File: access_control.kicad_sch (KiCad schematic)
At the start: 72 parts, among them J1 Conn_01x04_Pin, J10 Screw_Terminal_01x02, J2 Screw_Terminal_01x04, J3 Screw_Terminal_01x04, J4 Screw_Terminal_01x02, J5 Screw_Terminal_01x04, J6 Screw_Terminal_01x04, J7 Screw_Terminal_01x02, J8 Screw_Terminal_01x02, J9 Screw_Terminal_01x02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

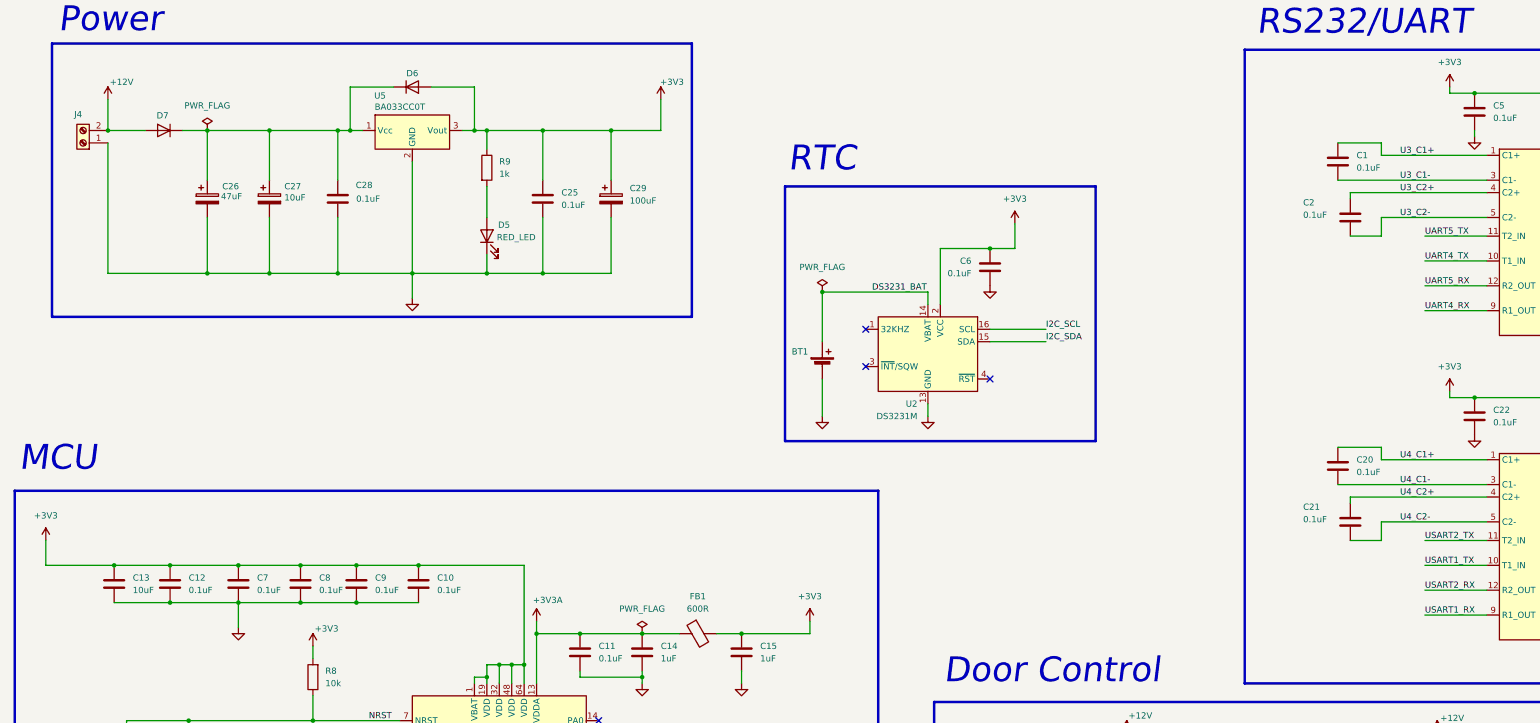
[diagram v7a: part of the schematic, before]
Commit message: Finished the PCB routing and placement of the components.
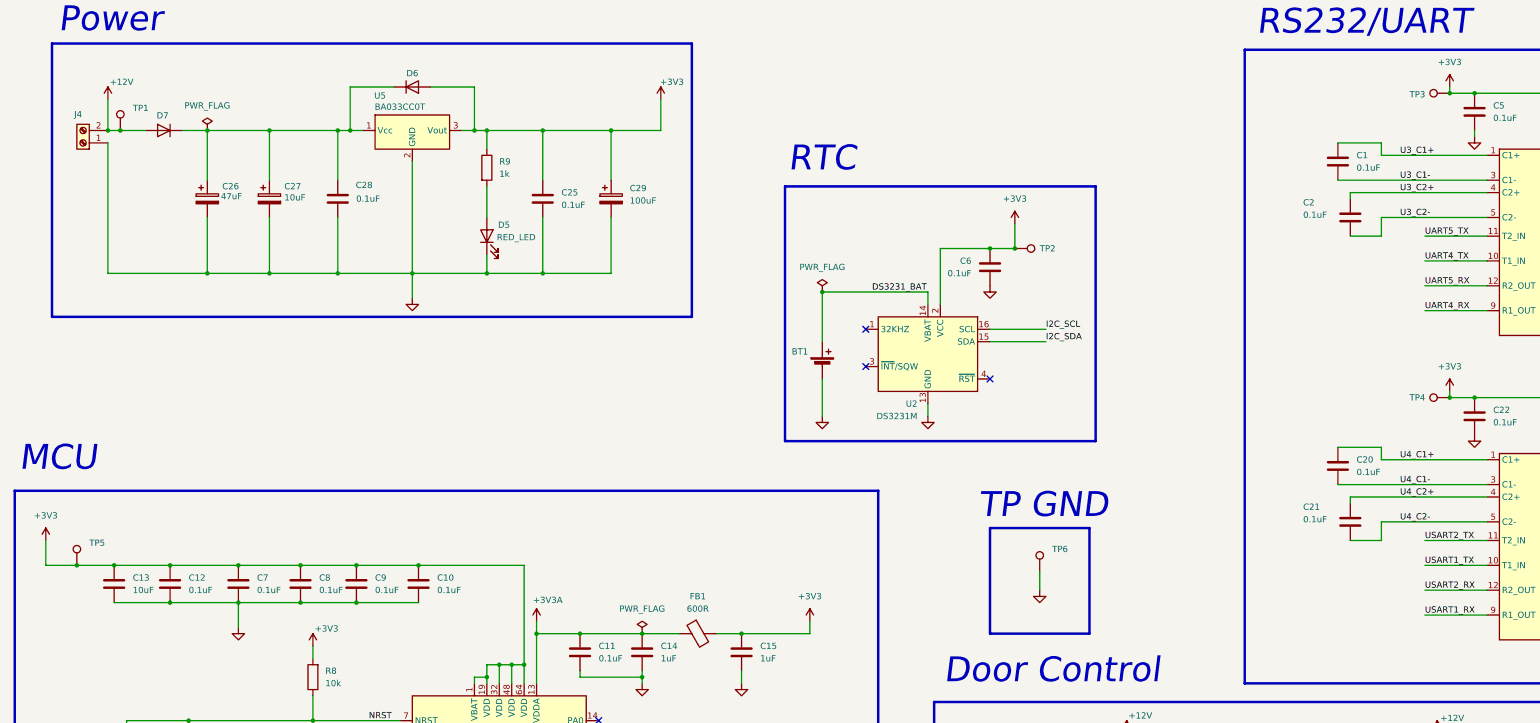
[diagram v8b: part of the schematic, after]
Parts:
- added TP1, TP2, TP3, TP4, TP5, TP6: TestPoint, TestPoint:TestPoint_Pad_D2.0mm, symbol Connector:TestPoint
- BT1: LCSC (none) -> C70377
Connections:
- net +12V: now also TP1.1
- net +3V3: now also TP2.1, TP3.1, TP4.1, TP5.1
- net GND: now also TP6.1
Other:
- note added: "TP GND"
